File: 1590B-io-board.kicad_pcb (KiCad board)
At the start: 2 copper layers, 54.8 x 46.5 mm, 5 parts, among them J1 ACJS-MHOM, J2 ACJS-MHOM, J3 Conn_01x04

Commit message: Add a few misc. adjustments
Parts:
- added D1: LED, LED_THT:LED_D3.0mm, F.Cu at (141.0, 95.8)
- added R1: R, Resistor_THT:R_Axial_DIN0204_L3.6mm_D1.6mm_P5.08mm_Horizontal, F.Cu at (137.8, 95.8)
- J3: footprint 1590:01x06_1.27mm_Ribbon_Pads -> 1590:01x06_2.54mm_Ribbon_Pads
- moved J3 5.75 mm to (142.4, 91.2)
- moved REF** 0.83 mm to (126.7, 137.3)
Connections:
- J3 pad 2: /FX_INPUT -> /OUTPUT_JACK_TIP
- J3 pad 3: /9V -> /FX_INPUT
- J3 pad 4: /OUTPUT_JACK_TIP -> /FX_OUTPUT
- J3 pad 5: /FX_OUTPUT -> GND
- J3 pad 6: GND -> /9V
- S1 pad 4: /9V -> Net-(D1-K)
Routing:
- net Net-(D1-K): track 0.00 -> 31.0 mm
- net /OUTPUT_JACK_TIP: track 42.6 -> 51.8 mm, vias 0 -> 1
- net /9V: track 29.5 -> 21.3 mm
- net Net-(D1-A): track 0.00 -> 7.24 mm
- net /FX_OUTPUT: track 30.6 -> 36.6 mm
- net /INPUT_JACK_TIP: track 38.9 -> 43.3 mm
- net /FX_INPUT: track 44.8 -> 47.8 mm
- net Net-(S1-Pad3): track 11.9 -> 12.5 mm
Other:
- board size 54.8 x 46.5 mm -> 54.8 x 53 mm
- board text added: "9V"
- board text added: "FX IN"
- board text added: "FX OUT"
- board text added: "GND"
- board text added: "IN"
- board text added: "OUT"
- board text added: "io board rev. 1.0"
- board text removed: "io board rev. 1"

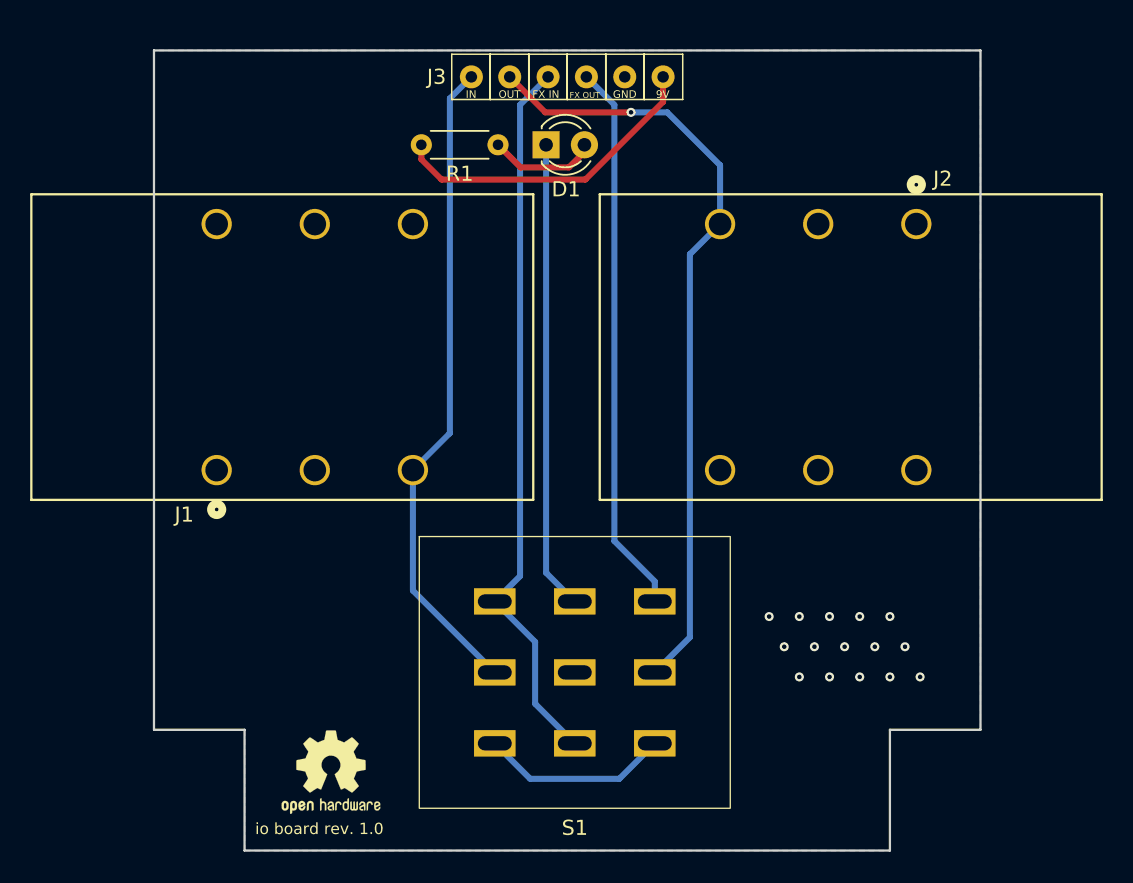
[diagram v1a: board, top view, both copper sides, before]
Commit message: Update board dimensions and jack layout
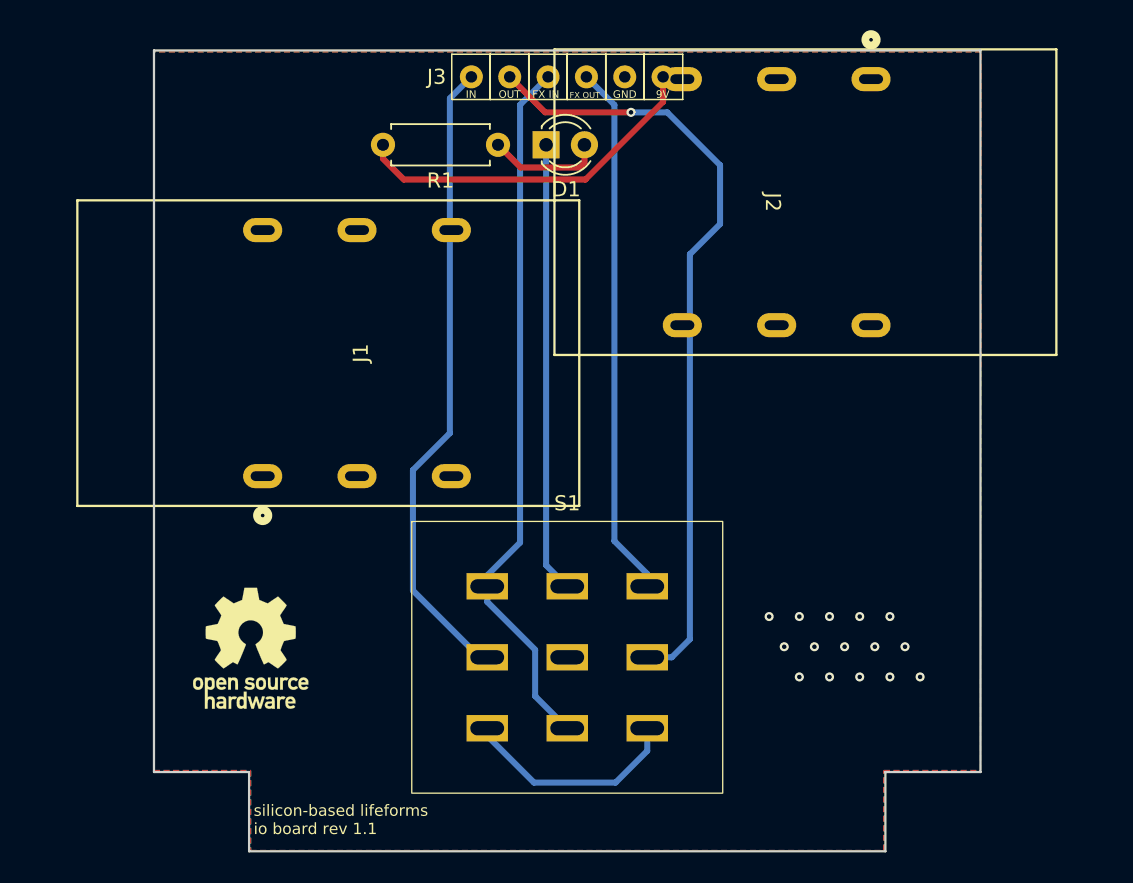
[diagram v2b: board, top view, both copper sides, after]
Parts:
- removed the REF** at (126.7, 137.3)
- added REF**: OSHW-Logo_7.5x8mm_SilkScreen, Symbol:OSHW-Logo_7.5x8mm_SilkScreen, F.Cu at (121.4, 129.1)
- J1, J2: footprint 1590:Amphenol_ACJS-IH -> KiCadAudio:Amphenol_ACJS-IH
- R1: footprint Resistor_THT:R_Axial_DIN0204_L3.6mm_D1.6mm_P5.08mm_Horizontal -> Resistor_THT:R_Axial_DIN0207_L6.3mm_D2.5mm_P7.62mm_Horizontal
- moved J2 10.1 mm to (162.5, 91.4)
- moved J1 3.07 mm to (122.2, 117.7)
- moved S1 1.12 mm to (142.4, 129.7)
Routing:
- net /9V: track 21.3 -> 23.8 mm
- net Net-(S1-Pad3): track 12.5 -> 14.8 mm
- net /FX_INPUT: track 47.8 -> 46.5 mm
- net Net-(D1-K): track 31.0 -> 29.8 mm
- net /FX_OUTPUT: track 36.6 -> 35.4 mm
- net /INPUT_JACK_TIP: track 43.3 -> 42.4 mm
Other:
- board size 54.8 x 53 mm -> 54.8 x 53.1 mm
- board text added: "silicon-based lifeforms io board rev 1.1"
- board text removed: "io board rev. 1.0"
